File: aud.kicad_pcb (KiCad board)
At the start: 2 copper layers, 19 x 37 mm, 17 parts, among them J1 AudioJack3_Ground, J3 Conn_01x12_Socket, U1 XTAD5212IRGER

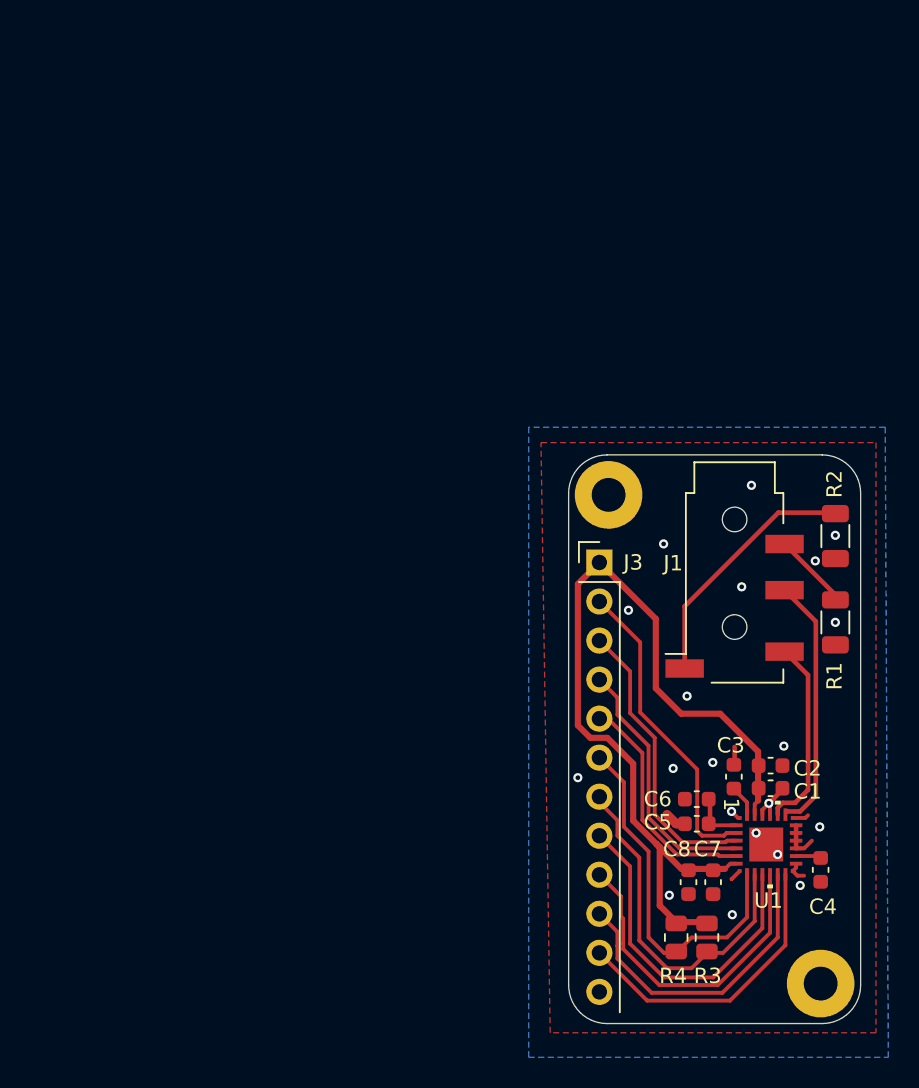
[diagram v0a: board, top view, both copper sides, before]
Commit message: Update to version 2
* Fixes the main mistake of not adding AC coupling caps.
* Adds a possibly working MICDET pin.
* Does not break out DOUT anymore.

Signed-off-by: Elvira Khabirova <lineprinter0@gmail.com>
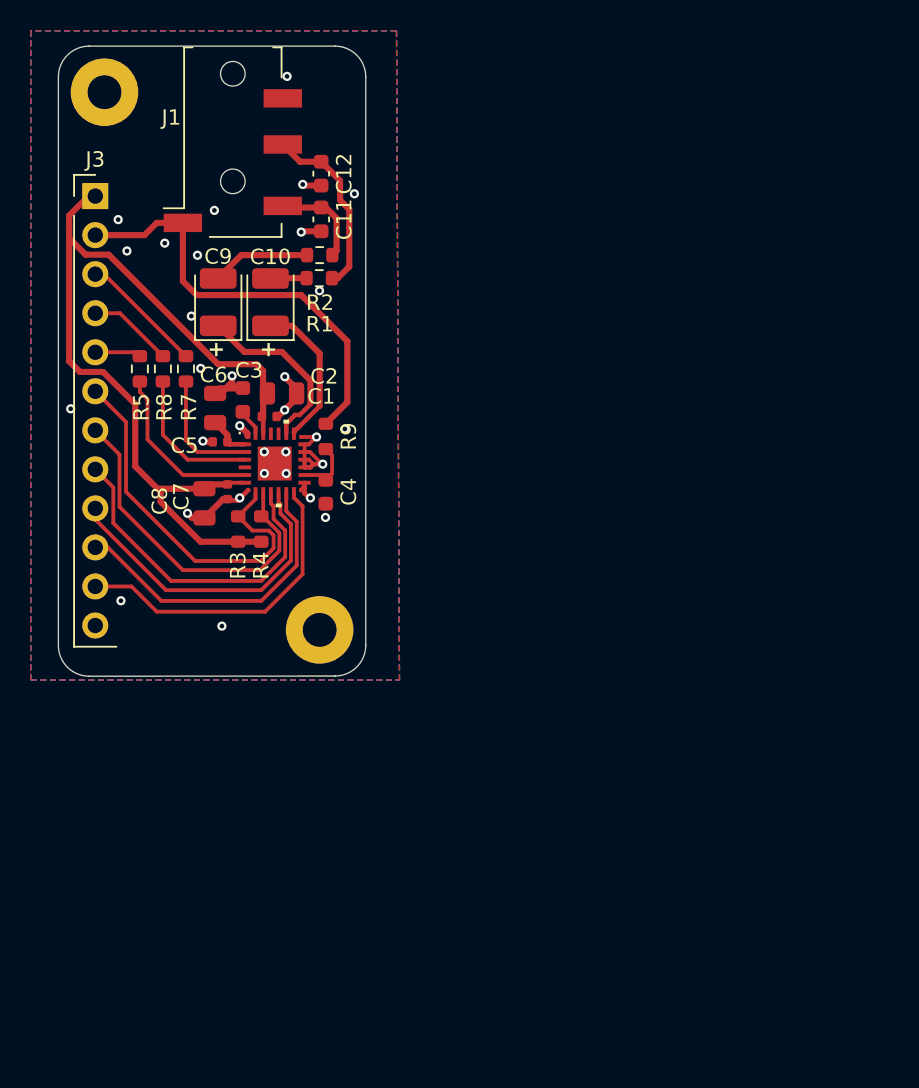
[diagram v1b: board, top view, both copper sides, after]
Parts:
- added C10: 47uF, Capacitor_Tantalum_SMD:CP_EIA-3528-21_Kemet-B, F.Cu at (93.8, 56.7)
- added C11: 47nF, Capacitor_SMD:C_0603_1608Metric, F.Cu at (97.1, 51.3)
- added C12: 47nF, Capacitor_SMD:C_0603_1608Metric, F.Cu at (97.1, 48.3)
- added C9: 47uF, Capacitor_Tantalum_SMD:CP_EIA-3528-21_Kemet-B, F.Cu at (90.4, 56.7)
- added R5: 22, Resistor_SMD:R_0603_1608Metric, F.Cu at (85.3, 61.0)
- added R7: 22, Resistor_SMD:R_0603_1608Metric, F.Cu at (88.3, 61.0)
- added R8: 22, Resistor_SMD:R_0603_1608Metric, F.Cu at (86.8, 61.0)
- added R9: 2.2k, Resistor_SMD:R_0603_1608Metric, F.Cu at (97.4, 65.4)
- C1, C5, C7: footprint Capacitor_SMD:C_0603_1608Metric -> Capacitor_SMD:C_0402_1005Metric
- C2, C6, C8: footprint Capacitor_SMD:C_0603_1608Metric -> Capacitor_SMD:C_0805_2012Metric
- R1, R2: value 0 -> 100; footprint Resistor_SMD:R_1206_3216Metric -> Resistor_SMD:R_0603_1608Metric
- R3, R4: footprint Resistor_SMD:R_0805_2012Metric -> Resistor_SMD:R_0603_1608Metric
- moved J1 43.7 mm to (91.3, 46.5)
- moved H1 42.0 mm to (83.0, 43.0)
- moved C1 40.6 mm to (93.7, 64.1)
- moved J3 40.5 mm to (82.4, 49.8)
- moved C7 40.5 mm to (91.0, 69.0)
- moved C4 40.5 mm to (97.4, 69.0)
- moved U1 40.5 mm to (94.1, 67.2)
- moved R3 40.5 mm to (91.7, 71.4), turned to -90 degrees
- moved C6 40.4 mm to (90.2, 63.5), turned to -90 degrees
- moved R1 40.4 mm to (97.0, 55.1), turned to 180 degrees
- moved C3 40.3 mm to (92.0, 63.0)
- moved C8 40.0 mm to (89.5, 69.8)
- moved C2 40.0 mm to (94.5, 62.6)
- moved H2 39.9 mm to (97.0, 78.0)
- moved C5 39.7 mm to (90.5, 65.8)
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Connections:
- net Net-(U1A-MICBIAS) renamed /MICBIAS
- J1 pad R1: Net-(U1A-OUT1M) -> /Jack_Right
- J1 pad R2: Net-(J1-PadR2) -> GND
- J1 pad S: Net-(J1-PadS) -> /Jack_Mic
- J1 pad T: Net-(U1A-OUT1P) -> /Jack_Left
- J3 pad 2: /BCLK -> /Jack_Mic
- J3 pad 3: /FSYNC -> /BCLK
- J3 pad 4: /DOUT -> /FSYNC
- R1 pad 1: Net-(J1-PadR2) -> /Jack_Right
- R1 pad 2: GND -> Net-(C10-Pad2)
- R2 pad 1: Net-(J1-PadS) -> /Jack_Left
- R2 pad 2: GND -> Net-(C9-Pad2)
- R3 pad 1: /SDA -> /SCL
- R4 pad 1: /SCL -> /SDA
- U1 pad 19: Net-(U1A-OUT1M) -> /OUT1M
- U1 pad 2: /BCLK -> Net-(U1A-BCLK)
- U1 pad 20: Net-(U1A-OUT1P) -> /OUT1P
- U1 pad 21: GND -> unconnected-(U1A-OUT2P-Pad21)
- U1 pad 22: GND -> unconnected-(U1A-OUT2M-Pad22)
- U1 pad 3: /FSYNC -> Net-(U1A-FSYNC)
- U1 pad 4: /DOUT -> unconnected-(U1A-DOUT-Pad4)
- U1 pad 5: /DIN -> Net-(U1A-DIN)
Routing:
- net /Jack_Mic: track 0.00 -> 28.1 mm
- net /DOUT: track 16.8 -> 0.00 mm
- net Net-(U1A-OUT1M): track 16.6 -> 0.00 mm
- net Net-(J1-PadS): track 15.9 -> 0.00 mm
- net GND: track 13.6 -> 27.9 mm, vias 20 -> 31
- net /FSYNC: track 18.9 -> 5.56 mm
- net Net-(U1A-OUT1P): track 12.5 -> 0.00 mm
- net /BCLK: track 20.3 -> 8.11 mm
- net /DIN: track 15.2 -> 3.01 mm
- net /Jack_Right: track 0.00 -> 12.0 mm
- net /OUT1P: track 0.00 -> 11.8 mm
- net Net-(U1A-DIN): track 0.00 -> 11.3 mm
- net /OUT1M: track 0.00 -> 9.86 mm
- net Net-(U1A-FSYNC): track 0.00 -> 9.48 mm
- net Net-(U1A-BCLK): track 0.00 -> 7.98 mm
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- added copper zone on In1.Cu, net GND
- added copper zone on In2.Cu, net GND
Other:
- board size 19 x 37 mm -> 20 x 41 mm
- copper layers 2 -> 4
- board text added: "+"
- board text added: "+3V3 MICDET BCLK FSYNC DIN SCL SDA GPIO1 GPIO2 GPO1 GPI1 GND"
- board text added: "TAD5112/TAD5212 breakout rev 2 by liney"
- board text removed: "1"
- board text removed: "TAD5212 breakout rev 1 by lineprinter R1 jumps Ring 2 to GND R2 jumps Sleeve to GND"
